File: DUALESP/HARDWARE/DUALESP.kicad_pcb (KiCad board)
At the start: 2 copper layers, 176.7 x 111.9 mm, 63 parts, among them J3 ESP_SERIAL_1, J4 ESP_SERIAL_0, J5 VGA, J6 Bus_ISA_8bit_CUSTOM, J7 MOUSE, J8 KEYBOARD, J9 AUDIO OUT, SW1 IO PORT ADDR, U1 74LS244, U10 74HC595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

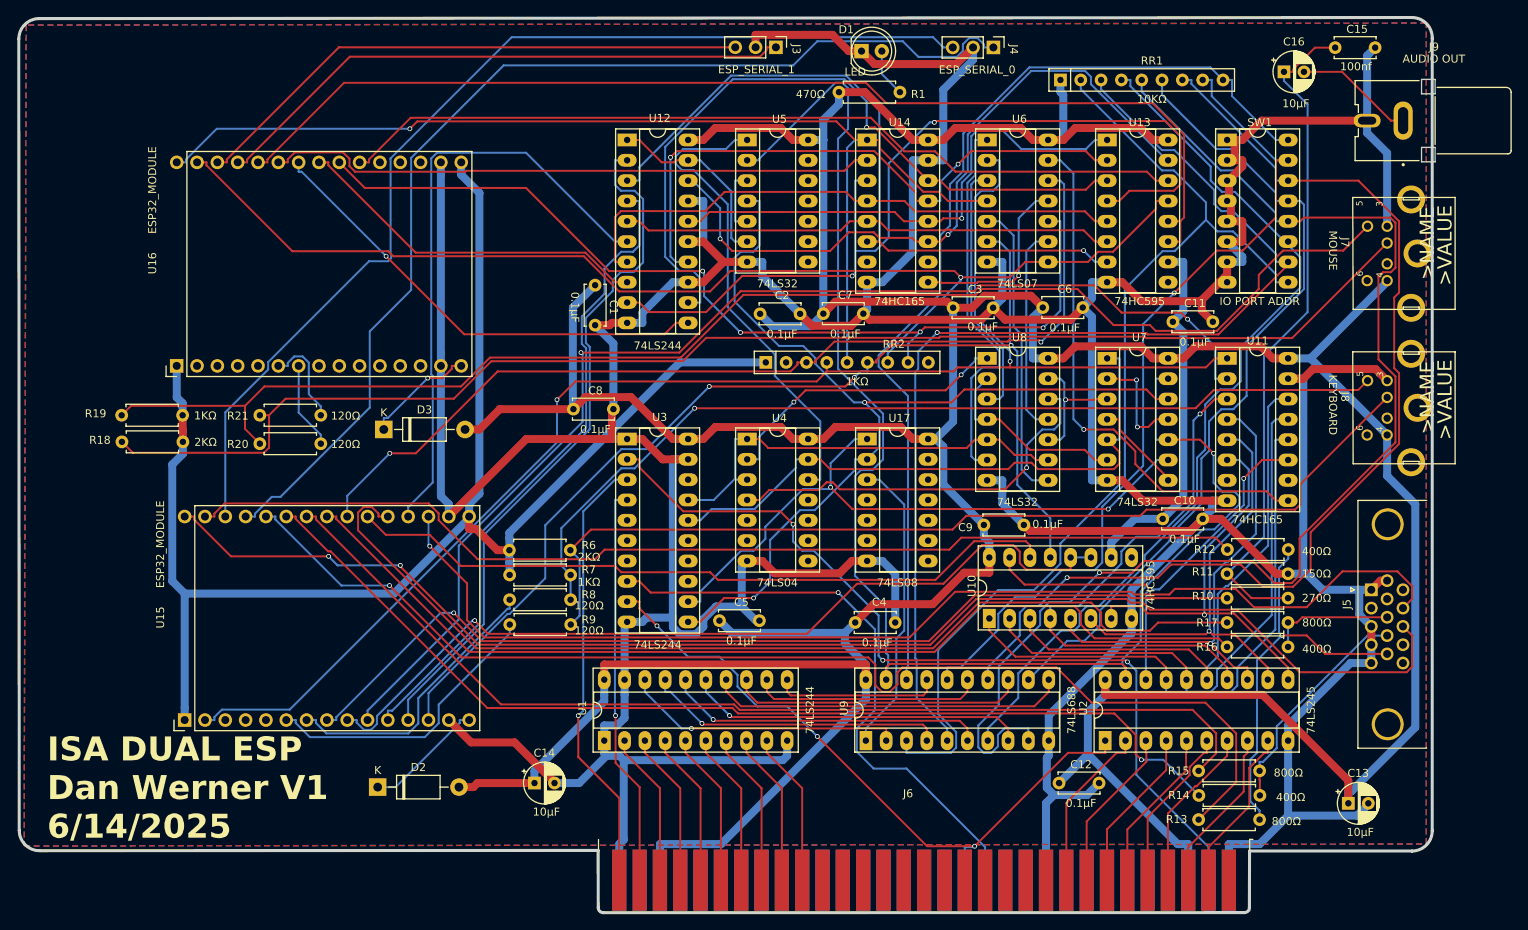
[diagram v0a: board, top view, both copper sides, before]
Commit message: fix ESP layout issues
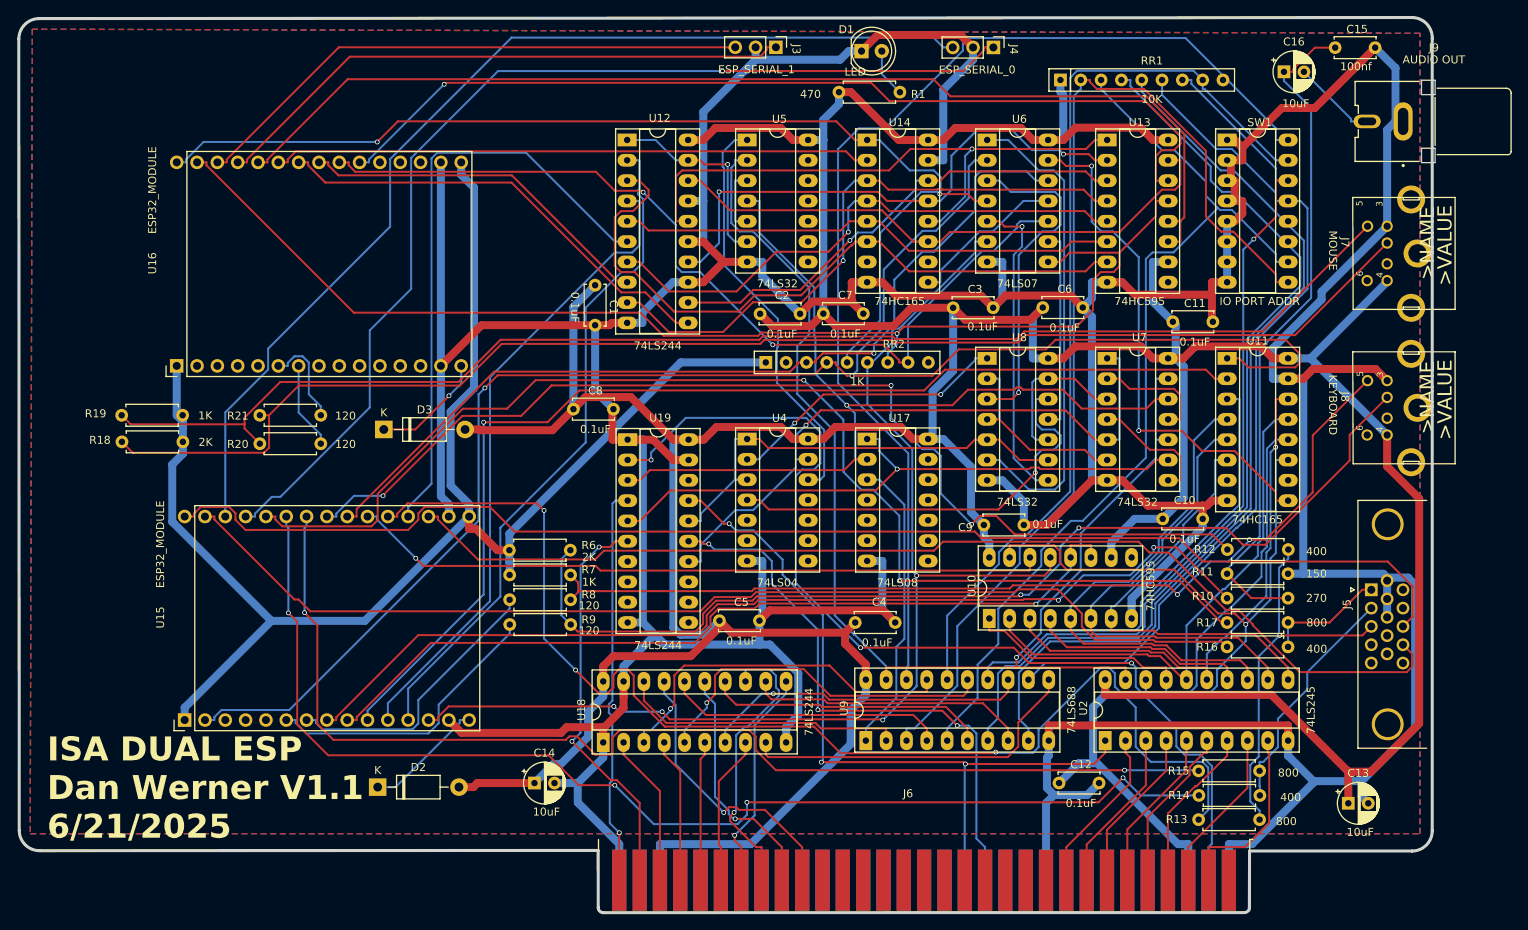
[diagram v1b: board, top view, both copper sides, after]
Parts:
- removed U1, U3: 74LS244, Custom:STD_DDW_DIP20
- added U18: 74LS244, Custom:STD_DDW_DIP20, F.Cu at (123.5, 121.4)
- added U19: 74LS244, Custom:STD_DDW_DIP20, F.Cu at (118.9, 98.9)
- C1, C10, C11, C12, C2, C3, C4, C5, C6, C7, C8, C9: value 0.1µF -> 0.1uF
- C13, C14, C16: value 10µF -> 10uF
- R1: value 470Ω -> 470
- R10: value 270Ω -> 270
- R11: value 150Ω -> 150
- R12, R14, R16: value 400Ω -> 400
- R13, R15, R17: value 800Ω -> 800
- R18, R6: value 2KΩ -> 2K
- R19, R7, RR2: value 1KΩ -> 1K
- R20, R21, R8, R9: value 120Ω -> 120
- RR1: value 10KΩ -> 10K
- moved J9 0.10 mm to (215.8, 38.9)
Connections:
- J5 pad 1: GND -> Net-(J5-Pad1)
- J5 pad 10: Net-(J5-Pad10) -> unconnected-(J5-Pad10)
- J5 pad 12: VGA_VSYNC -> unconnected-(J5-Pad12)
- J5 pad 14: unconnected-(J5-Pad14) -> VGA_VSYNC
- J5 pad 2: unconnected-(J5-Pad2) -> Net-(J5-Pad2)
- J5 pad 3: GND -> Net-(J5-Pad3)
- J5 pad 4: GND -> unconnected-(J5-Pad4)
- J5 pad 5: GND -> unconnected-(J5-Pad5)
- J5 pad 7: unconnected-(J5-Pad7) -> GND
- J5 pad 8: Net-(J5-Pad8) -> GND
- J5 pad 9: Net-(J5-Pad9) -> unconnected-(J5-Pad9)
- R12 pad 1: VGA_R1 -> VGA_B1
- R12 pad 2: Net-(J5-Pad10) -> Net-(J5-Pad3)
- R13 pad 1: VGA_R0 -> VGA_B0
- R13 pad 2: Net-(J5-Pad10) -> Net-(J5-Pad3)
- R14 pad 2: Net-(J5-Pad9) -> Net-(J5-Pad2)
- R15 pad 2: Net-(J5-Pad9) -> Net-(J5-Pad2)
- R16 pad 1: VGA_B1 -> VGA_R1
- R16 pad 2: Net-(J5-Pad8) -> Net-(J5-Pad1)
- R17 pad 1: VGA_B0 -> VGA_R0
- R17 pad 2: Net-(J5-Pad8) -> Net-(J5-Pad1)
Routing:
- net Net-(J5-Pad10): track 50.6 -> 0.00 mm, vias 1 -> 0
- net Net-(J5-Pad3): track 0.00 -> 48.2 mm, vias 0 -> 1
- net Net-(RR1-R4): track 159.3 -> 114.3 mm, vias 1 -> 0
- net bD4: track 113.7 -> 75.5 mm, vias 2 -> 1
- net ~{ESP0_WR}: track 182.3 -> 215.0 mm
- net bD3: track 90.7 -> 60.3 mm
- net ~{CS_ESP}: track 185.9 -> 156.3 mm
- net Net-(J5-Pad2): track 0.00 -> 29.5 mm
- net Net-(J5-Pad9): track 28.3 -> 0.00 mm
- net Net-(RR1-R6): track 135.1 -> 107.0 mm
- net VGA_B0: track 126.8 -> 152.5 mm, vias 0 -> 3
- net Net-(U18-O3b): track 20.9 -> 45.4 mm, vias 0 -> 1
- net GND: track 780.4 -> 803.6 mm
- net Net-(U10-QA): track 57.5 -> 79.9 mm, vias 2 -> 1
- net Net-(RR1-R2): track 136.8 -> 118.1 mm, vias 1 -> 0
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- added copper zone on B.Cu, net (none)
- added copper zone on F.Cu, net (none)
- removed copper zone on B.Cu, net GND
- removed copper zone on F.Cu, net GND
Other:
- board text added: "ISA DUAL ESP Dan Werner V1.1 6/21/2025"
- board text removed: "ISA DUAL ESP Dan Werner V1 6/14/2025"

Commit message: ESPIO updates
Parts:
- C1, C10, C11, C12, C2, C3, C4, C5, C6, C7, C8, C9: value 0.1uF -> 0.1µF
- C13, C14, C16: value 10uF -> 10µF
- R1: value 470 -> 470Ω
- R10: value 270 -> 270Ω
- R11: value 150 -> 150Ω
- R12, R14, R16: value 400 -> 400Ω
- R13, R15, R17: value 800 -> 800Ω
- R18, R6: value 2K -> 2KΩ
- R19, R7, RR2: value 1K -> 1KΩ
- R20, R21, R8, R9: value 120 -> 120Ω
- RR1: value 10K -> 10KΩ
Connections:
- U10 pad 1: Net-(U10-QB) -> bD1
- U10 pad 15: Net-(U10-QA) -> bD0
- U10 pad 2: Net-(U10-QC) -> bD2
- U10 pad 3: Net-(U10-QD) -> bD3
- U10 pad 4: Net-(U10-QE) -> bD4
- U10 pad 5: Net-(U10-QF) -> bD5
- U10 pad 6: Net-(U10-QG) -> bD6
- U10 pad 7: Net-(U10-QH) -> bD7
- U11 pad 11: Net-(U10-QA) -> bD0
- U11 pad 12: Net-(U10-QB) -> bD1
- U11 pad 13: Net-(U10-QC) -> bD2
- U11 pad 14: Net-(U10-QD) -> bD3
- U11 pad 3: Net-(U10-QE) -> bD4
- U11 pad 4: Net-(U10-QF) -> bD5
- U11 pad 5: Net-(U10-QG) -> bD6
- U11 pad 6: Net-(U10-QH) -> bD7
- U2 pad 11: Net-(U10-QH) -> bD7
- U2 pad 12: Net-(U10-QG) -> bD6
- U2 pad 13: Net-(U10-QF) -> bD5
- U2 pad 14: Net-(U10-QE) -> bD4
- U2 pad 15: Net-(U10-QD) -> bD3
- U2 pad 16: Net-(U10-QC) -> bD2
- U2 pad 17: Net-(U10-QB) -> bD1
- U2 pad 18: Net-(U10-QA) -> bD0
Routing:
- net bD3: track 60.3 -> 192.4 mm, vias 1 -> 3
- net bD0: track 72.2 -> 193.1 mm, vias 0 -> 4
- net bD2: track 67.9 -> 179.1 mm, vias 2 -> 5
- net bD1: track 75.1 -> 183.5 mm, vias 1 -> 5
- net bD4: track 75.5 -> 178.9 mm, vias 1 -> 3
- net bD5: track 69.1 -> 171.9 mm, vias 1 -> 4
- net bD6: track 63.0 -> 164.3 mm, vias 0 -> 1
- net bD7: track 84.9 -> 181.0 mm, vias 0 -> 5
- net VCC: track 649.2 -> 735.2 mm, vias 0 -> 18
- net GND: track 803.6 -> 889.2 mm, vias 0 -> 14
- net Net-(U10-QA): track 79.9 -> 0.00 mm, vias 1 -> 0
- net Net-(U10-QE): track 75.2 -> 0.00 mm
- net Net-(U10-QB): track 69.2 -> 0.00 mm
- net Net-(U10-QD): track 67.4 -> 0.00 mm, vias 1 -> 0
- net Net-(U10-QC): track 65.0 -> 0.00 mm
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- added copper zone on B.Cu, net GND
- added copper zone on F.Cu, net GND
- removed copper zone on B.Cu, net (none)
- removed copper zone on F.Cu, net (none)
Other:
- board text added: "ISA DUAL ESP Dan Werner V1.2 6/28/2025"
- board text removed: "ISA DUAL ESP Dan Werner V1.1 6/21/2025"

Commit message: ESPIO updates
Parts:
- removed D1: LED, Custom:STD_DDW_LED5
- removed R1: 470Ω, Custom:STD_DDW_RESISTOR
- U11, U14: value 74HC165 -> 74ACT165
- U19: value 74LS244 -> 74ALS244
- U5, U7, U8: value 74LS32 -> 74F32
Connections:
- J5 pad 10: unconnected-(J5-Pad10) -> GND
- J5 pad 5: unconnected-(J5-Pad5) -> GND
- RR2 pad 4: ~{ESP0_WR} -> unconnected-(RR2-R3-Pad4)
- RR2 pad 5: ~{ESP1_WR} -> unconnected-(RR2-R4-Pad5)
- RR2 pad 6: ~{ESP0_RD} -> unconnected-(RR2-R5-Pad6)
- RR2 pad 7: ~{ESP1_RD} -> unconnected-(RR2-R6-Pad7)
- U6 pad 1: Net-(U6-Pad1) -> unconnected-(U6-Pad1)
- U6 pad 2: ~{ESP0_WR} -> unconnected-(U6-Pad2)
- U6 pad 3: Net-(U6-Pad3) -> unconnected-(U6-Pad3)
- U6 pad 4: ~{ESP1_WR} -> unconnected-(U6-Pad4)
- U6 pad 5: Net-(U6-Pad5) -> unconnected-(U6-Pad5)
- U6 pad 6: ~{ESP0_RD} -> unconnected-(U6-Pad6)
- U6 pad 8: ~{ESP1_RD} -> unconnected-(U6-Pad8)
- U6 pad 9: Net-(U6-Pad9) -> unconnected-(U6-Pad9)
- U8 pad 11: Net-(U6-Pad9) -> ~{ESP1_RD}
- U8 pad 3: Net-(U6-Pad3) -> ~{ESP1_WR}
- U8 pad 6: Net-(U6-Pad1) -> ~{ESP0_WR}
- U8 pad 8: Net-(U6-Pad5) -> ~{ESP0_RD}
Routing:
- net Net-(U6-Pad1): track 44.9 -> 0.00 mm
- net Net-(U6-Pad5): track 37.7 -> 0.00 mm
- net Net-(U6-Pad3): track 31.4 -> 0.00 mm
- net Net-(U6-Pad9): track 29.5 -> 0.00 mm
- net ~{ESP1_RD}: track 148.2 -> 165.6 mm, vias 3 -> 4
- net ~{ESP0_WR}: track 206.3 -> 193.0 mm, vias 3 -> 5
- net ~{ESP0_RD}: track 157.2 -> 144.8 mm
- net Net-(D1-A): track 6.07 -> 0.00 mm
- net GND: track 889.2 -> 890.5 mm, vias 14 -> 15
- net ESP1_IN: track 127.5 -> 126.9 mm
- net VCC: vias 18 -> 19
